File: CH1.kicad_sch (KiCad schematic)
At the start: 23 parts, among them IC101 TS12A4516DBVR, J101 CH1, SW101 AC/DC, U102 OPA356xxDBV, U104 OPA356xxDBV

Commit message: v3 initial schematic
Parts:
- removed C104, C107: 1u, Capacitor_SMD:C_0402_1005Metric_Pad0.74x0.62mm_HandSolder, symbol Device:C_Small
- removed IC101: TS12A4516DBVR, SOT95P280X145-5N, symbol TS12A4516:TS12A4516DBVR
- removed R101: 1k, Resistor_SMD:R_0402_1005Metric_Pad0.72x0.64mm_HandSolder, symbol Device:R_Small_US
- added C110 (x2): 1u, Capacitor_SMD:C_0402_1005Metric_Pad0.74x0.62mm_HandSolder, symbol Device:C_Small
- added R104: 100k, Resistor_SMD:R_0805_2012Metric_Pad1.20x1.40mm_HandSolder, symbol Device:R_Small_US
- added R108: 1k, Resistor_SMD:R_0402_1005Metric_Pad0.72x0.64mm_HandSolder, symbol Device:R_Small_US
- added R108: 402, Resistor_SMD:R_0402_1005Metric_Pad0.72x0.64mm_HandSolder, symbol Device:R_Small_US
- added SW101: AC/DC, Button_Switch_THT:SW_DIP_SPSTx01_Slide_9.78x4.72mm_W7.62mm_P2.54mm, symbol Switch:SW_SPST
- added U203: TLP176AM, Package_SO:MFSOP6-4_4.4x3.6mm_P1.27mm, symbol Relay_SolidState:TLP175A
- added U204: DG612, Package_SO:TSSOP-16_4.4x5mm_P0.65mm, symbol Analog_Switch:DG442xY
- C101: value 10n -> 270p; Part Number (none) -> GRM1555C1H271JA01J
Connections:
- net GND: now also C110.2, C110.2, U203.3, U204.3, U204.5 (GND); no longer C101.2
- net V+: now also C110.1, SW101.1 (A), U204.13 (V+)
- net V-: now also C110.1, U204.4 (V-)
- net at C103.1, J101.1 (In): now also U203.6; no longer D101.2 (A2)
- net at C103.2, R104.1, U102.3 (+): now also C101.1, D101.2 (A2), R104.1, U203.4
- net at SW101.2 (B): now also R108.2; no longer C101.1
- new net: R108.1, U203.1
- new net: C101.2, R104.2, U204.2
- new net: R108.1, U204.1
- new net: R108.2, SW101.2 (B)
- no-connect marks 0 -> 10
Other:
- moved on the sheet: C103, D101, J101, R104, SW101

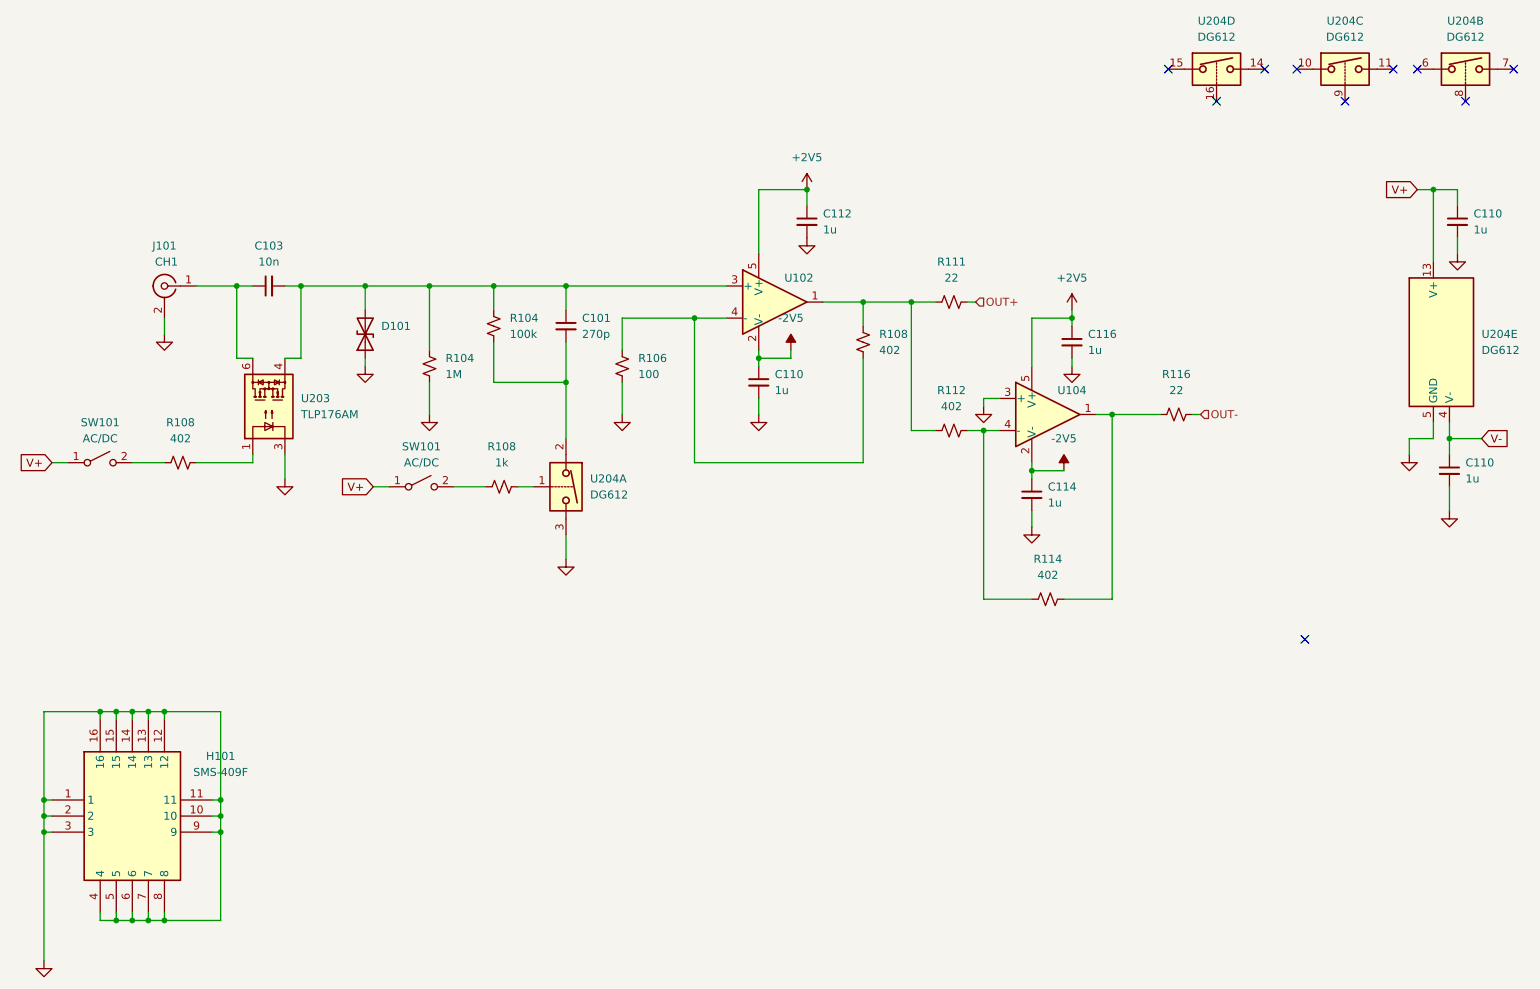
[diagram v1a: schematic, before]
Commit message: changed mux
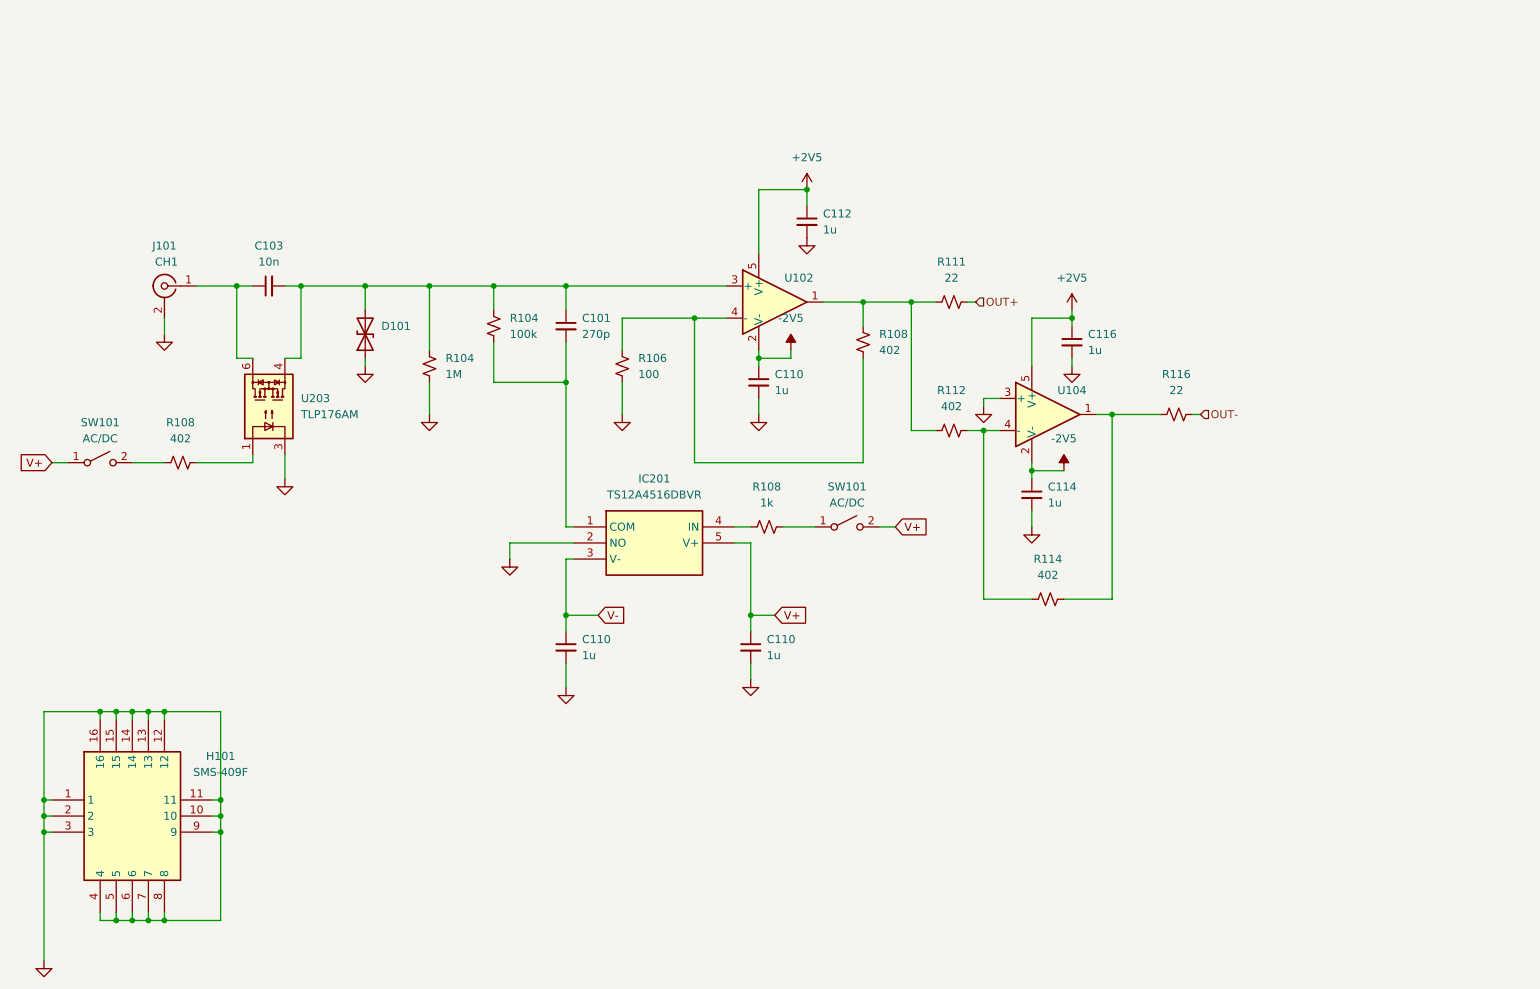
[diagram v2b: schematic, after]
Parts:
- removed U204: DG612, Package_SO:TSSOP-16_4.4x5mm_P0.65mm, symbol Analog_Switch:DG442xY
- added IC201: TS12A4516DBVR, SOT95P280X145-5N, symbol TS12A4516:TS12A4516DBVR
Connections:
- net GND: now also IC201.2 (NO)
- net V+: now also SW101.2 (B), IC201.5 (V+); no longer SW101.1 (A)
- net V-: now also IC201.3 (V-)
- net at C101.2, R104.2: now also IC201.1 (COM)
- net at R108.1: now also SW101.1 (A)
- net at R108.2: now also IC201.4 (IN); no longer SW101.2 (B)
- no-connect marks 10 -> 0
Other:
- moved on the sheet: C110, R108, SW101

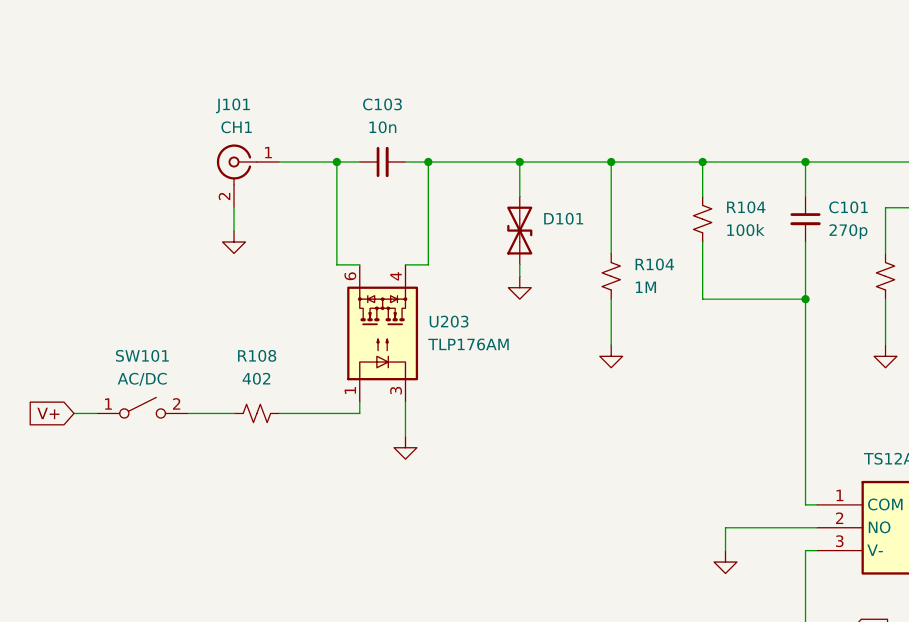
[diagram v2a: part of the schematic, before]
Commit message: Ch1 Layout
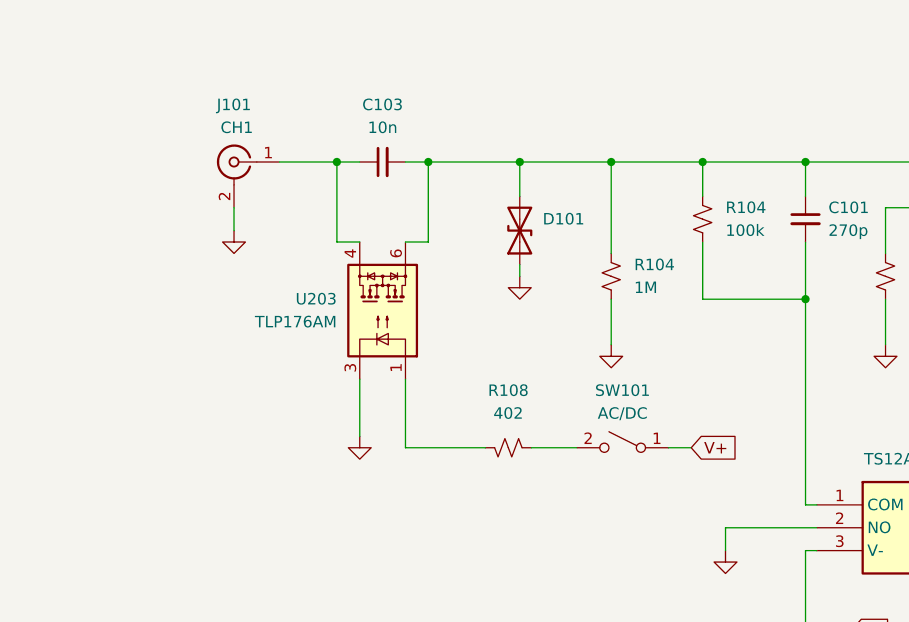
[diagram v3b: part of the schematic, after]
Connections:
- net at C101.1, C103.2, D101.2 (A2)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: now also U203.6; no longer U203.4
- net at C103.1, J101.1 (In): now also U203.4; no longer U203.6
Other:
- moved on the sheet: R108, SW101, U203
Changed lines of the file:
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@@
     (stroke (width 0) (type default))
   )
-  (wire (pts (xy 81.28 73.66) (xy 83.82 73.66))
+  (wire (pts (xy 81.28 71.12) (xy 83.82 71.12))
     (stroke (width 0) (type default))
   )
@@
     (stroke (width 0) (type default))
   )
+  (wire (pts (xy 81.28 86.36) (xy 81.28 93.98))
+    (stroke (width 0) (type default))
+  )
   (wire (pts (xy 59.69 129.54) (xy 62.23 129.54))
     (stroke (width 0) (type default))
@@
     (stroke (width 0) (type default))
   )
-  (wire (pts (xy 73.66 62.23) (xy 73.66 73.66))
+  (wire (pts (xy 73.66 62.23) (xy 73.66 71.12))
     (stroke (width 0) (type default))
   )
@@
     (stroke (width 0) (type default))
   )
-  (wire (pts (xy 44.45 90.17) (xy 46.99 90.17))
+  (wire (pts (xy 113.03 93.98) (xy 110.49 93.98))
     (stroke (width 0) (type default))
   )
@@
     (stroke (width 0) (type default))
   )
-  (wire (pts (xy 76.2 90.17) (xy 76.2 88.9))
-    (stroke (width 0) (type default))
-  )
   (wire (pts (xy 180.34 64.77) (xy 180.34 85.09))
     (stroke (width 0) (type default))
@@
     (stroke (width 0) (type default))
   )
-  (wire (pts (xy 83.82 62.23) (xy 83.82 73.66))
+  (wire (pts (xy 83.82 62.23) (xy 83.82 71.12))
     (stroke (width 0) (type default))
   )
@@
     (stroke (width 0) (type default))
   )
-  (wire (pts (xy 76.2 73.66) (xy 73.66 73.66))
-    (stroke (width 0) (type default))
-  )
-  (wire (pts (xy 57.15 90.17) (xy 62.23 90.17))
+  (wire (pts (xy 76.2 71.12) (xy 73.66 71.12))
+    (stroke (width 0) (type default))
+  )
+  (wire (pts (xy 100.33 93.98) (xy 95.25 93.98))
     (stroke (width 0) (type default))
   )
@@
     (stroke (width 0) (type default))
   )
+  (wire (pts (xy 76.2 86.36) (xy 76.2 92.71))
+    (stroke (width 0) (type default))
+  )
   (wire (pts (xy 189.23 85.09) (xy 191.77 85.09))
     (stroke (width 0) (type default))
   )
-  (wire (pts (xy 67.31 90.17) (xy 76.2 90.17))
+  (wire (pts (xy 90.17 93.98) (xy 81.28 93.98))
     (stroke (width 0) (type default))
   )
@@
   )
   (wire (pts (xy 71.12 148.59) (xy 71.12 162.56))
-    (stroke (width 0) (type default))
-  )
-  (wire (pts (xy 81.28 88.9) (xy 81.28 92.71))
     (stroke (width 0) (type default))
   )
@@
     )
   )
-  (global_label "V+" (shape input) (at 44.45 90.17 180) (fields_autoplaced)
-    (effects (font (size 1.27 1.27)) (justify right))
-    (property "Intersheetrefs" "${INTERSHEET_REFS}" (at 38.8038 90.17 0)
-      (effects (font (size 1.27 1.27)) (justify right) hide)
+  (global_label "V+" (shape input) (at 113.03 93.98 0) (fields_autoplaced)
+    (effects (font (size 1.27 1.27)) (justify left))
+    (property "Intersheetrefs" "${INTERSHEET_REFS}" (at 118.6762 93.98 0)
+      (effects (font (size 1.27 1.27)) (justify left) hide)
     )
   )
@@
     (effects (font (size 1.27 1.27)) (justify left))
   )
-  (symbol (lib_id "Relay_SolidState:TLP175A") (at 78.74 81.28 90) (unit 1)
-    (in_bom yes) (on_board yes) (dnp no) (fields_autoplaced)
-    (property "Reference" "U203" (at 83.82 80.01 90)
+  (symbol (lib_id "Relay_SolidState:TLP175A") (at 78.74 78.74 270) (mirror x) (unit 1)
+    (in_bom yes) (on_board yes) (dnp no)
+    (property "Reference" "U203" (at 73.66 77.47 90)
       (effects (font (size 1.27 1.27)) (justify right))
     )
-    (property "Value" "TLP176AM" (at 83.82 82.55 90)
+    (property "Value" "TLP176AM" (at 73.66 80.01 90)
       (effects (font (size 1.27 1.27)) (justify right))
     )
-    (property "Footprint" "Package_SO:MFSOP6-4_4.4x3.6mm_P1.27mm" (at 86.36 81.28 0)
+    (property "Footprint" "Package_SO:MFSOP6-4_4.4x3.6mm_P1.27mm" (at 71.12 78.74 0)
       (effects (font (size 1.27 1.27) italic) hide)
     )
-    (property "Datasheet" "https://toshiba.semicon-storage.com/info/docget.jsp?did=13665&prodName=TLP175A" (at 78.74 81.28 0)
+    (property "Datasheet" "https://toshiba.semicon-storage.com/info/docget.jsp?did=13665&prodName=TLP175A" (at 78.74 78.74 0)
       (effects (font (size 1.27 1.27)) (justify left) hide)
     )
@@
     )
   )
-  (symbol (lib_id "Device:R_Small_US") (at 64.77 90.17 270) (unit 1)
-    (in_bom yes) (on_board yes) (dnp no) (fields_autoplaced)
-    (property "Reference" "R108" (at 64.77 83.82 90)
-      (effects (font (size 1.27 1.27)))
-    )
-    (property "Value" "402" (at 64.77 86.36 90)
-      (effects (font (size 1.27 1.27)))
-    )
-    (property "Footprint" "Resistor_SMD:R_0402_1005Metric_Pad0.72x0.64mm_HandSolder" (at 64.77 90.17 0)
-      (effects (font (size 1.27 1.27)) hide)
-    )
-    (property "Datasheet" "~" (at 64.77 90.17 0)
+  (symbol (lib_id "Device:R_Small_US") (at 92.71 93.98 90) (mirror x) (unit 1)
+    (in_bom yes) (on_board yes) (dnp no) (fields_autoplaced)
+    (property "Reference" "R108" (at 92.71 87.63 90)
+      (effects (font (size 1.27 1.27)))
+    )
+    (property "Value" "402" (at 92.71 90.17 90)
+      (effects (font (size 1.27 1.27)))
+    )
+    (property "Footprint" "Resistor_SMD:R_0402_1005Metric_Pad0.72x0.64mm_HandSolder" (at 92.71 93.98 0)
+      (effects (font (size 1.27 1.27)) hide)
+    )
+    (property "Datasheet" "~" (at 92.71 93.98 0)
       (effects (font (size 1.27 1.27)) hide)
     )
@@
     )
   )
-  (symbol (lib_id "Switch:SW_SPST") (at 52.07 90.17 0) (unit 1)
+  (symbol (lib_id "Switch:SW_SPST") (at 105.41 93.98 0) (mirror y) (unit 1)
     (in_bom yes) (on_board yes) (dnp no)
-    (property "Reference" "SW101" (at 52.07 83.82 0)
-      (effects (font (size 1.27 1.27)))
-    )
-    (property "Value" "AC/DC" (at 52.07 86.36 0)
-      (effects (font (size 1.27 1.27)))
-    )
-    (property "Footprint" "Button_Switch_THT:SW_DIP_SPSTx01_Slide_9.78x4.72mm_W7.62mm_P2.54mm" (at 52.07 90.17 0)
-      (effects (font (size 1.27 1.27)) hide)
-    )
-    (property "Datasheet" "~" (at 52.07 90.17 0)
-      (effects (font (size 1.27 1.27)) hide)
-    )
-    (property "Part Number" "" (at 52.07 90.17 0)
+    (property "Reference" "SW101" (at 105.41 87.63 0)
+      (effects (font (size 1.27 1.27)))
+    )
+    (property "Value" "AC/DC" (at 105.41 90.17 0)
+      (effects (font (size 1.27 1.27)))
+    )
+    (property "Footprint" "Button_Switch_THT:SW_DIP_SPSTx01_Slide_9.78x4.72mm_W7.62mm_P2.54mm" (at 105.41 93.98 0)
+      (effects (font (size 1.27 1.27)) hide)
+    )
+    (property "Datasheet" "~" (at 105.41 93.98 0)
+      (effects (font (size 1.27 1.27)) hide)
+    )
+    (property "Part Number" "" (at 105.41 93.98 0)
       (effects (font (size 1.27 1.27)) hide)
     )
@@
     )
   )
-  (symbol (lib_id "power:GND") (at 81.28 92.71 0) (unit 1)
-    (in_bom yes) (on_board yes) (dnp no) (fields_autoplaced)
-    (property "Reference" "#PWR0110" (at 81.28 99.06 0)
-      (effects (font (size 1.27 1.27)) hide)
-    )
-    (property "Value" "GND" (at 81.28 97.79 0)
-      (effects (font (size 1.27 1.27)) hide)
-    )
-    (property "Footprint" "" (at 81.28 92.71 0)
-      (effects (font (size 1.27 1.27)) hide)
-    )
-    (property "Datasheet" "" (at 81.28 92.71 0)
-      (effects (font (size 1.27 1.27)) hide)
-    )
+  (symbol (lib_id "power:GND") (at 76.2 92.71 0) (unit 1)
+    (in_bom yes) (on_board yes) (dnp no) (fields_autoplaced)
+    (property "Reference" "#PWR0110" (at 76.2 99.06 0)
+      (effects (font (size 1.27 1.27)) hide)
+    )
+    (property "Value" "GND" (at 76.2 97.79 0)
+      (effects (font (size 1.27 1.27)) hide)
+    )
+    (property "Footprint" "" (at 76.2 92.71 0)
+      (effects (font (size 1.27 1.27)) hide)
+    )
+    (property "Datasheet" "" (at 76.2 92.71 0)
+      (effects (font (size 1.27 1.27)) hide)
+    )

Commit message: v3 done
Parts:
- added C101: (select on test), Capacitor_SMD:C_0402_1005Metric_Pad0.74x0.62mm_HandSolder, symbol Device:C_Small
- SW101: value AC/DC -> /10
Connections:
- net at C101.1, C103.2, D101.2 (A2)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: now also C101.1
- net at C101.2, IC201.1 (COM), R104.2: now also C101.2
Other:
- moved on the sheet: C101, C103, C110, D101, IC201, J101, R104, R108, SW101, U203
